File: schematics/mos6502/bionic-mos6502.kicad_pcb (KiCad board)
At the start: 2 copper layers, 27.9 x 68.6 mm, 8 parts, among them J1 Bionic-P135, J2 Bionic-P245, U1 W65C816S, U2 11AA010-I/TT

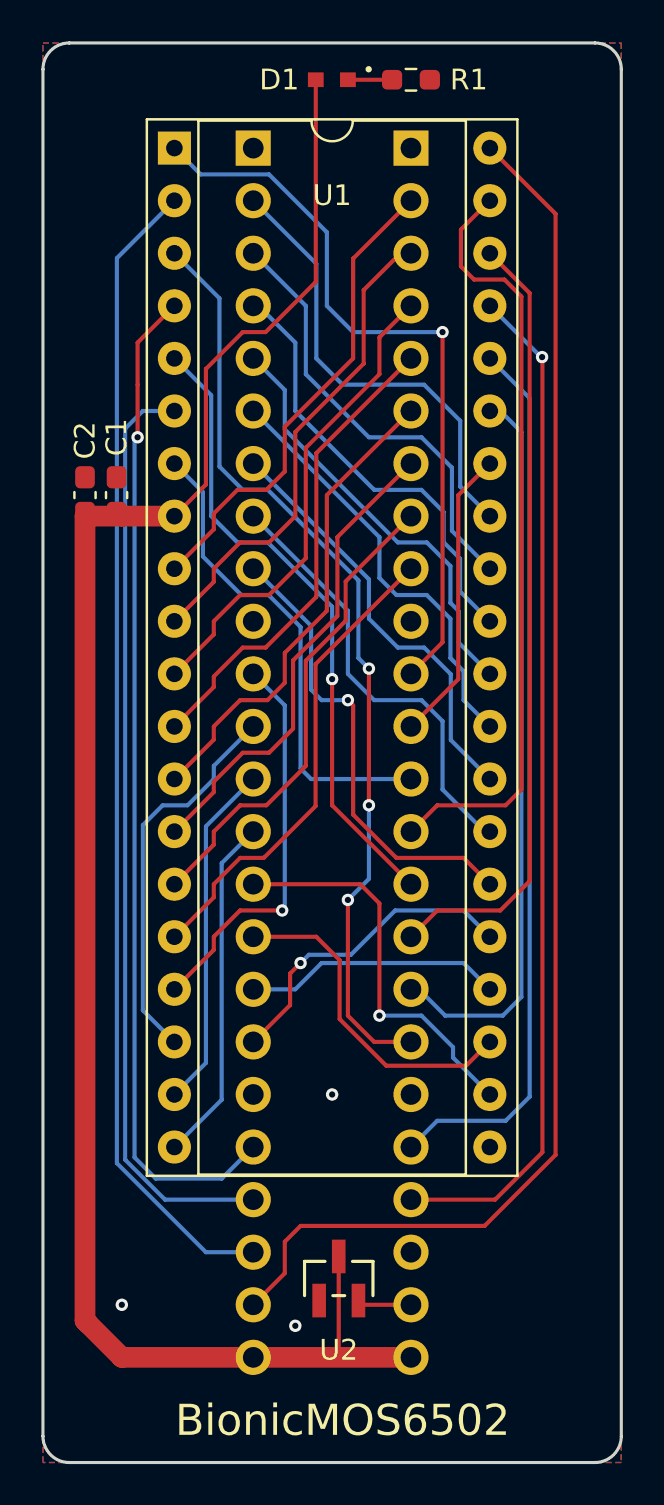
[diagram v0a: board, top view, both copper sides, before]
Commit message: [MOS6502] Fix EEPROM pinout
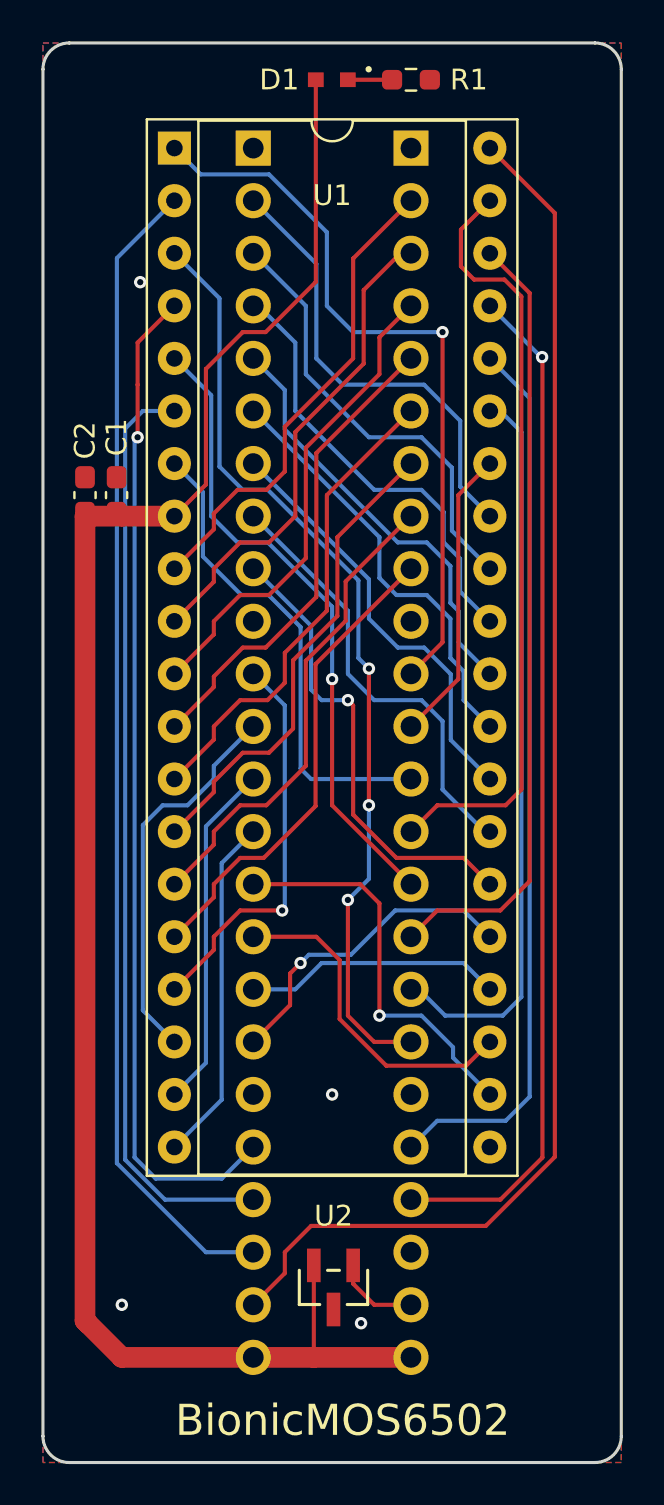
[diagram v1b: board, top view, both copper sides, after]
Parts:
- moved U2 0.50 mm to (115.0, 130.1), turned to 180 degrees
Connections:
- U2 pad 1: GND -> Net-(J2-P57)
- U2 pad 2: Net-(J2-P57) -> VCC
- U2 pad 3: VCC -> GND
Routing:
- net Net-(J2-P57): track 2.62 -> 4.10 mm
- net GND: vias 3 -> 4
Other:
- board text added: "Rev. 9"
- board text removed: "Rev. 8"
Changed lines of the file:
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@@
   (title_block
     (title "BionicMOS6502")
-    (date "2024-05-10")
-    (rev "8")
+    (date "2024-11-01")
+    (rev "9")
     (company "Tadashi G. Takaoka")
   )
@@
   (net 47 "Net-(D1-K)")
   (footprint "0-LocalLibrary:SOT-23_MC_MCH-M" (layer "F.Cu")
-    (at 115.29 129.69)
+    (at 115.035999 130.121 180)
     (descr "Microchip 11AAxxx-I/TT UNI/O 1Kbit Serial EEPROM")
     (property "Sheetfile" "bionic-mos6502.kicad_sch")
@@
         (effects (font (size 1 1) (thickness 0.15)))
     )
-    (fp_text value "11AA010-I/TT" (at 0 0 unlocked) (layer "F.Fab")
+    (fp_text value "11AA010-I/TT" (at 0 0 180 unlocked) (layer "F.Fab")
         (effects (font (size 1 1) (thickness 0.15)))
     )
-    (fp_text user "${REFERENCE}" (at 0 0 unlocked) (layer "F.Fab")
+    (fp_text user "${REFERENCE}" (at 0 0 180 unlocked) (layer "F.Fab")
         (effects (font (size 1 1) (thickness 0.15)))
     )
@@
     (fp_circle (center -1.270999 0.446) (end -1.143999 0.446)
       (stroke (width 0.0254) (type solid)) (fill none) (layer "F.Fab"))
-    (pad "1" smd rect (at -0.950001 1.066) (size 0.6604 1.6256) (layers "F.Cu" "F.Paste" "F.Mask")
+    (pad "1" smd rect (at -0.950001 1.066 180) (size 0.6604 1.6256) (layers "F.Cu" "F.Paste" "F.Mask")
+      (net 43 "Net-(J2-P57)") (pinfunction "SCIO") (pintype "bidirectional"))
+    (pad "2" smd rect (at 0.950001 1.066 180) (size 0.6604 1.6256) (layers "F.Cu" "F.Paste" "F.Mask")
+      (net 1 "VCC") (pinfunction "VCC") (pintype "power_in"))
+    (pad "3" smd rect (at 0 -1.066 180) (size 0.6604 1.6256) (layers "F.Cu" "F.Paste" "F.Mask")
       (net 2 "GND") (pinfunction "VSS") (pintype "power_in"))
-    (pad "2" smd rect (at 0.950001 1.066) (size 0.6604 1.6256) (layers "F.Cu" "F.Paste" "F.Mask")
-      (net 43 "Net-(J2-P57)") (pinfunction "SCIO") (pintype "bidirectional"))
-    (pad "3" smd rect (at 0 -1.066) (size 0.6604 1.6256) (layers "F.Cu" "F.Paste" "F.Mask")
-      (net 1 "VCC") (pinfunction "VCC") (pintype "power_in"))
     (model "${KIPRJMOD}/0-LocalLibrary/SOT-23_MC_MCH.step"
       (offset (xyz 0 0 0))
@@
   (gr_line (start 102.27 138.58) (end 127.67 138.58)
     (stroke (width 0.15) (type default)) (layer "Edge.Cuts"))
-  (gr_text "Rev. 8" (at 102.27 136.802) (layer "B.SilkS")
+  (gr_text "Rev. 9" (at 102.27 136.802) (layer "B.SilkS")
     (effects (font (size 1 1)) (justify right mirror))
   )
@@
     )
   )
+  (segment (start 114.081 133.5) (end 111.16 133.5) (width 1) (layer "F.Cu") (net 1))
   (segment (start 110.652 83.97) (end 108.874 85.748) (width 0.2) (layer "F.Cu") (net 1))
+  (segment (start 114.085998 133.495002) (end 114.081 133.5) (width 0.2) (layer "F.Cu") (net 1))
   (segment (start 114.1826 81.543746) (end 111.756346 83.97) (width 0.2) (layer "F.Cu") (net 1))
   (segment (start 111.756346 83.97) (end 110.652 83.97) (width 0.2) (layer "F.Cu") (net 1))
   (segment (start 114.1826 71.778) (end 114.1826 81.543746) (width 0.2) (layer "F.Cu") (net 1))
   (segment (start 103.032 131.722) (end 103.032 92.86) (width 1) (layer "F.Cu") (net 1))
+  (segment (start 118.78 133.5) (end 114.081 133.5) (width 1) (layer "F.Cu") (net 1))
   (segment (start 108.874 85.748) (end 108.874 91.336) (width 0.2) (layer "F.Cu") (net 1))
   (segment (start 114.183 71.778) (end 114.1826 71.778) (width 0.2) (layer "F.Cu") (net 1))
   (segment (start 104.7095 92.86) (end 104.556 92.7065) (width 0.2) (layer "F.Cu") (net 1))
-  (segment locked (start 118.78 133.5) (end 111.16 133.5) (width 1) (layer "F.Cu") (net 1))
-  (segment (start 115.29 133.5) (end 115.29 128.624) (width 0.2) (layer "F.Cu") (net 1))
   (segment (start 104.81 133.5) (end 103.159 131.849) (width 1) (layer "F.Cu") (net 1))
   (segment (start 103.159 131.849) (end 103.032 131.722) (width 1) (layer "F.Cu") (net 1))
@@
   (segment locked (start 103.032 92.86) (end 104.81 92.86) (width 1) (layer "F.Cu") (net 1))
   (segment (start 103.032 92.86) (end 103.032 92.7065) (width 0.2) (layer "F.Cu") (net 1))
+  (segment (start 114.085998 129.055) (end 114.085998 133.495002) (width 0.2) (layer "F.Cu") (net 1))
+  (via (at 105.699 81.557) (size 0.6) (drill 0.3) (layers "F.Cu" "B.Cu") (free) (net 2))
   (via (at 114.97 120.8) (size 0.6) (drill 0.3) (layers "F.Cu" "B.Cu") (free) (net 2))
   (via (at 104.81 130.96) (size 0.6) (drill 0.3) (layers "F.Cu" "B.Cu") (free) (net 2))
-  (via (at 113.192 131.976) (size 0.6) (drill 0.3) (layers "F.Cu" "B.Cu") (free) (net 2))
+  (via (at 116.367 131.849) (size 0.6) (drill 0.3) (layers "F.Cu" "B.Cu") (free) (net 2))
   (segment (start 115.624 97.921) (end 113.7 99.845) (width 0.2) (layer "F.Cu") (net 4))
   (segment (start 110.525 106.83) (end 109.255 108.1) (width 0.2) (layer "F.Cu") (net 4))
@@
   (segment (start 104.972 123.952314) (end 106.899686 125.88) (width 0.2) (layer "B.Cu") (net 38))
   (segment (start 106.899686 125.88) (end 111.16 125.88) (width 0.2) (layer "B.Cu") (net 38))
-  (segment (start 125.765 78.255) (end 122.59 75.08) (width 0.2) (layer "F.Cu") (net 39))
-  (segment (start 111.16 130.96) (end 112.684 129.436) (width 0.2) (layer "F.Cu") (net 39))
-  (segment (start 125.765 123.721) (end 125.765 78.255) (width 0.2) (layer "F.Cu") (net 39))
-  (segment (start 122.336 127.15) (end 125.765 123.721) (width 0.2) (layer "F.Cu") (net 39))
-  (segment (start 112.684 129.436) (end 112.684 127.912) (width 0.2) (layer "F.Cu") (net 39))
-  (segment (start 113.446 127.15) (end 122.336 127.15) (width 0.2) (layer "F.Cu") (net 39))
-  (segment (start 112.684 127.912) (end 113.446 127.15) (width 0.2) (layer "F.Cu") (net 39))
-  (segment (start 125.13 85.1925) (end 125.13 123.594) (width 0.2) (layer "F.Cu") (net 40))
+  (segment (start 113.954 127.15) (end 112.684 128.42) (width 0.2) (layer "F.Cu") (net 39))
+  (segment (start 122.59 75.08) (end 125.73 78.22) (width 0.2) (layer "F.Cu") (net 39))
+  (segment (start 125.73 123.813686) (end 122.393686 127.15) (width 0.2) (layer "F.Cu") (net 39))
+  (segment (start 112.684 128.42) (end 112.684 129.436) (width 0.2) (layer "F.Cu") (net 39))
+  (segment (start 122.393686 127.15) (end 113.954 127.15) (width 0.2) (layer "F.Cu") (net 39))
+  (segment (start 112.684 129.436) (end 111.16 130.96) (width 0.2) (layer "F.Cu") (net 39))
+  (segment (start 125.73 78.22) (end 125.73 123.813686) (width 0.2) (layer "F.Cu") (net 39))
   (segment (start 125.114 85.1765) (end 125.13 85.1925) (width 0.2) (layer "F.Cu") (net 40))
-  (segment (start 125.13 123.594) (end 122.844 125.88) (width 0.2) (layer "F.Cu") (net 40))
-  (segment (start 122.844 125.88) (end 118.78 125.88) (width 0.2) (layer "F.Cu") (net 40))
+  (segment (start 125.13 85.1925) (end 125.13 123.848) (width 0.2) (layer "F.Cu") (net 40))
+  (segment (start 123.098 125.88) (end 118.78 125.88) (width 0.2) (layer "F.Cu") (net 40))
+  (segment (start 125.13 123.848) (end 123.098 125.88) (width 0.2) (layer "F.Cu") (net 40))
   (via (at 125.114 85.1765) (size 0.6) (drill 0.3) (layers "F.Cu" "B.Cu") (net 40))
   (segment (start 125.114 85.1765) (end 125.0665 85.1765) (width 0.2) (layer "B.Cu") (net 40))
@@
   (segment (start 120.05 122.07) (end 123.352 122.07) (width 0.2) (layer "B.Cu") (net 41))
   (segment (start 124.514 120.908) (end 124.514 87.164) (width 0.2) (layer "B.Cu") (net 41))
-  (segment (start 116.444 130.96) (end 116.24 130.756) (width 0.2) (layer "F.Cu") (net 43))
-  (segment (start 118.78 130.96) (end 116.444 130.96) (width 0.2) (layer "F.Cu") (net 43))
+  (segment (start 117.002 130.96) (end 118.78 130.96) (width 0.2) (layer "F.Cu") (net 43))
+  (segment (start 115.986 129.944) (end 117.002 130.96) (width 0.2) (layer "F.Cu") (net 43))
+  (segment (start 115.986 129.055) (end 115.986 129.944) (width 0.2) (layer "F.Cu") (net 43))
   (segment (start 115.732 71.778) (end 117.8675 71.778) (width 0.2) (layer "F.Cu") (net 47))
   (zone (net 2) (net_name "GND") (layers "F&B.Cu") (hatch edge 0.5)

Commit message: [MOS6502] Shrink board size
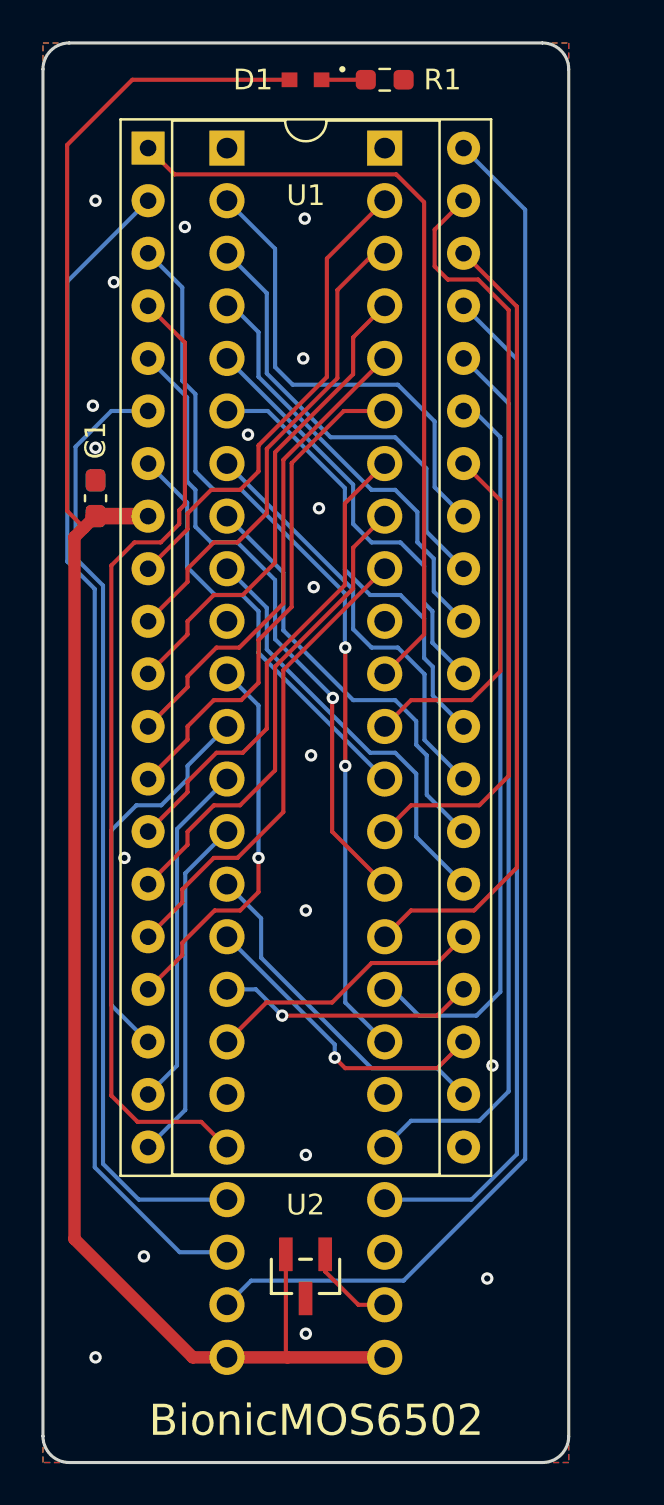
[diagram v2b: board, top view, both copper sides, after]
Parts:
- C2: moved to B.Cu
- moved U2 1.45 mm to (113.7, 129.6)
- moved D1 1.27 mm to (113.7, 71.8)
- moved J1 1.27 mm to (109.9, 75.1)
- moved J2 1.27 mm to (117.5, 75.1)
- moved R1 1.27 mm to (117.5, 71.8)
- moved U1 1.27 mm to (106.1, 75.1)
- moved C1 1.03 mm to (103.5, 92.0)
- moved C2 0.53 mm to (103.5, 92.0)
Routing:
- net VCC: track 89.0 -> 93.9 mm
- net /P41: track 14.3 -> 17.5 mm
- net /P42: track 23.6 -> 20.7 mm
- net /P34: track 19.1 -> 16.8 mm, vias 1 -> 0
- net /P40: track 35.9 -> 38.0 mm, vias 1 -> 0
- net /P37: track 15.5 -> 13.5 mm, vias 1 -> 0
- net /P17: track 22.6 -> 20.7 mm, vias 1 -> 0
- net /P47: track 45.4 -> 43.6 mm, vias 3 -> 2
- net /P35: track 16.2 -> 15.0 mm, vias 0 -> 1
- net /P24: track 23.3 -> 24.4 mm
- net /P14: track 20.8 -> 22.0 mm
- net /P51: track 45.0 -> 46.1 mm
- net /P50: track 48.7 -> 47.7 mm, vias 1 -> 0
- net /P52: track 56.0 -> 57.0 mm
- net /P53: track 68.2 -> 67.4 mm
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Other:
- board size 27.9 x 68.6 mm -> 25.4 x 68.6 mm

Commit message: [MOS6502] Improve PCB layout
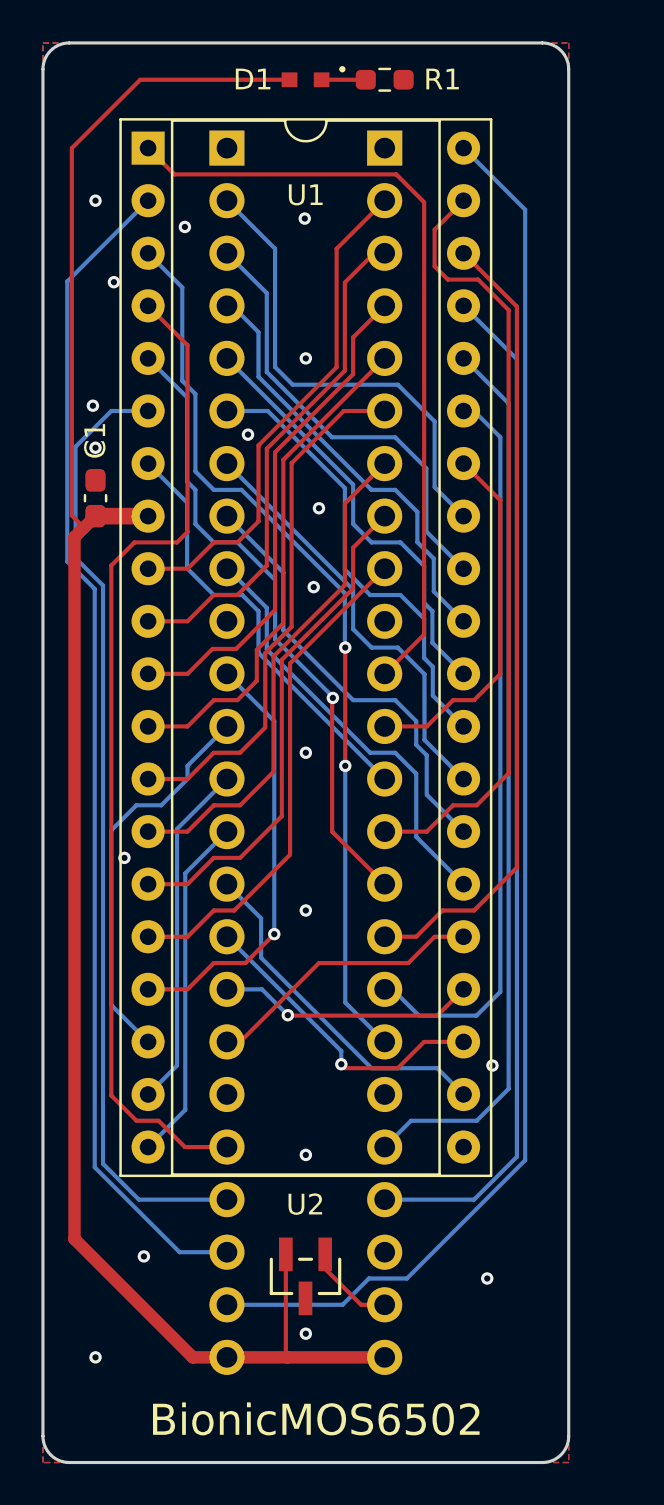
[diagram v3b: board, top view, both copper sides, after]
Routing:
- net /P30: track 18.8 -> 20.7 mm
- net /P23: track 23.2 -> 24.3 mm
- net /P21: track 24.1 -> 25.2 mm
- net /P26: track 23.3 -> 24.4 mm
- net /P25: track 23.3 -> 24.4 mm
- net /P24: track 24.4 -> 25.5 mm
- net /P27: track 23.2 -> 24.2 mm
- net /P20: track 23.3 -> 24.3 mm
- net /P22: track 23.3 -> 24.3 mm
- net /P50: track 47.7 -> 48.3 mm

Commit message: [schematics] Update LED footprint
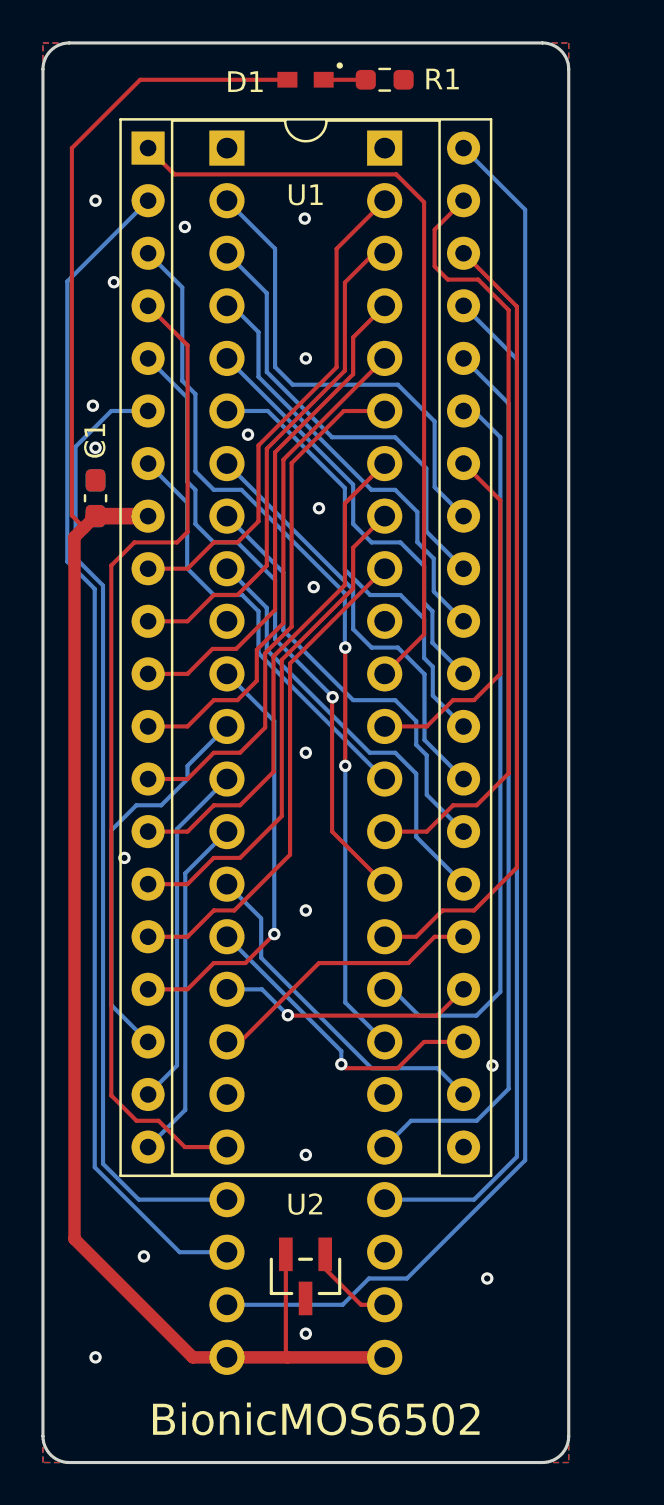
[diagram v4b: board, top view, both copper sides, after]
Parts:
- D1: footprint 0-LocalLibrary:LED_CSL1901UW1_ROM -> 0-LocalLibrary:LED_CSL1901UW1_ROM-M
